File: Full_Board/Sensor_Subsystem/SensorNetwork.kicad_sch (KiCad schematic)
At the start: 34 parts, among them IC5 CD74HC4051PWT, IC6 CD74HC4051PWT, J12 OQ0432500000G, J13 OQ0432500000G, J14 OQ0432500000G, J15 OQ0432500000G, J16 OQ0432500000G, J17 OQ0432500000G, J18 OQ0432500000G, J19 OQ0432500000G, U13 UCLAMP3301H.TCT, U14 UCLAMP3301H.TCT

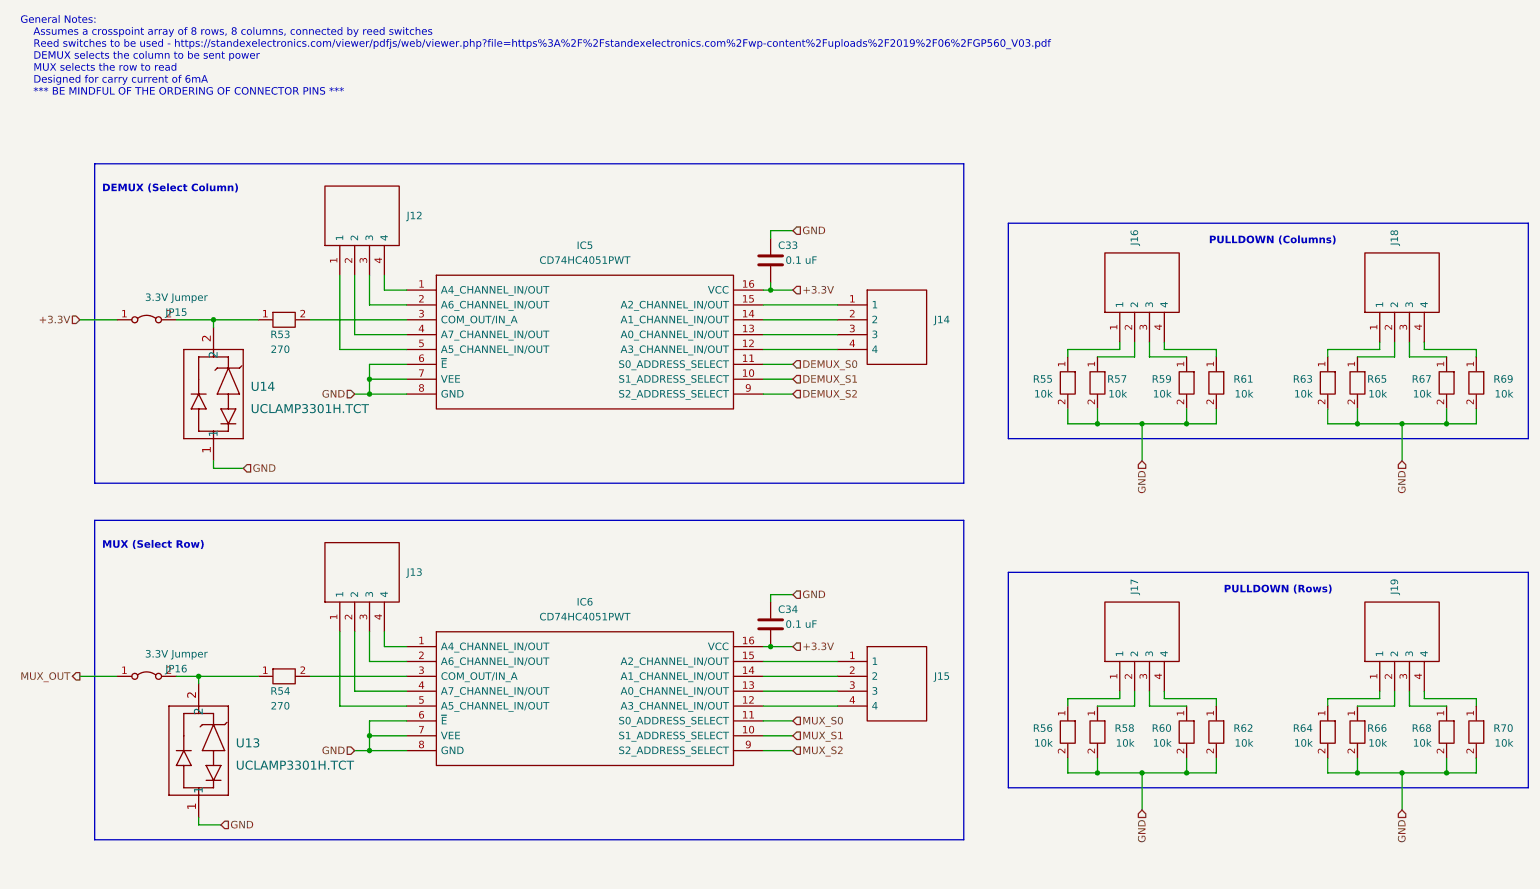
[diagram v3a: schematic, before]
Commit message: Replace small resistors/capacitors with through-hole; fix DRC aside from electromagnet and MUXes
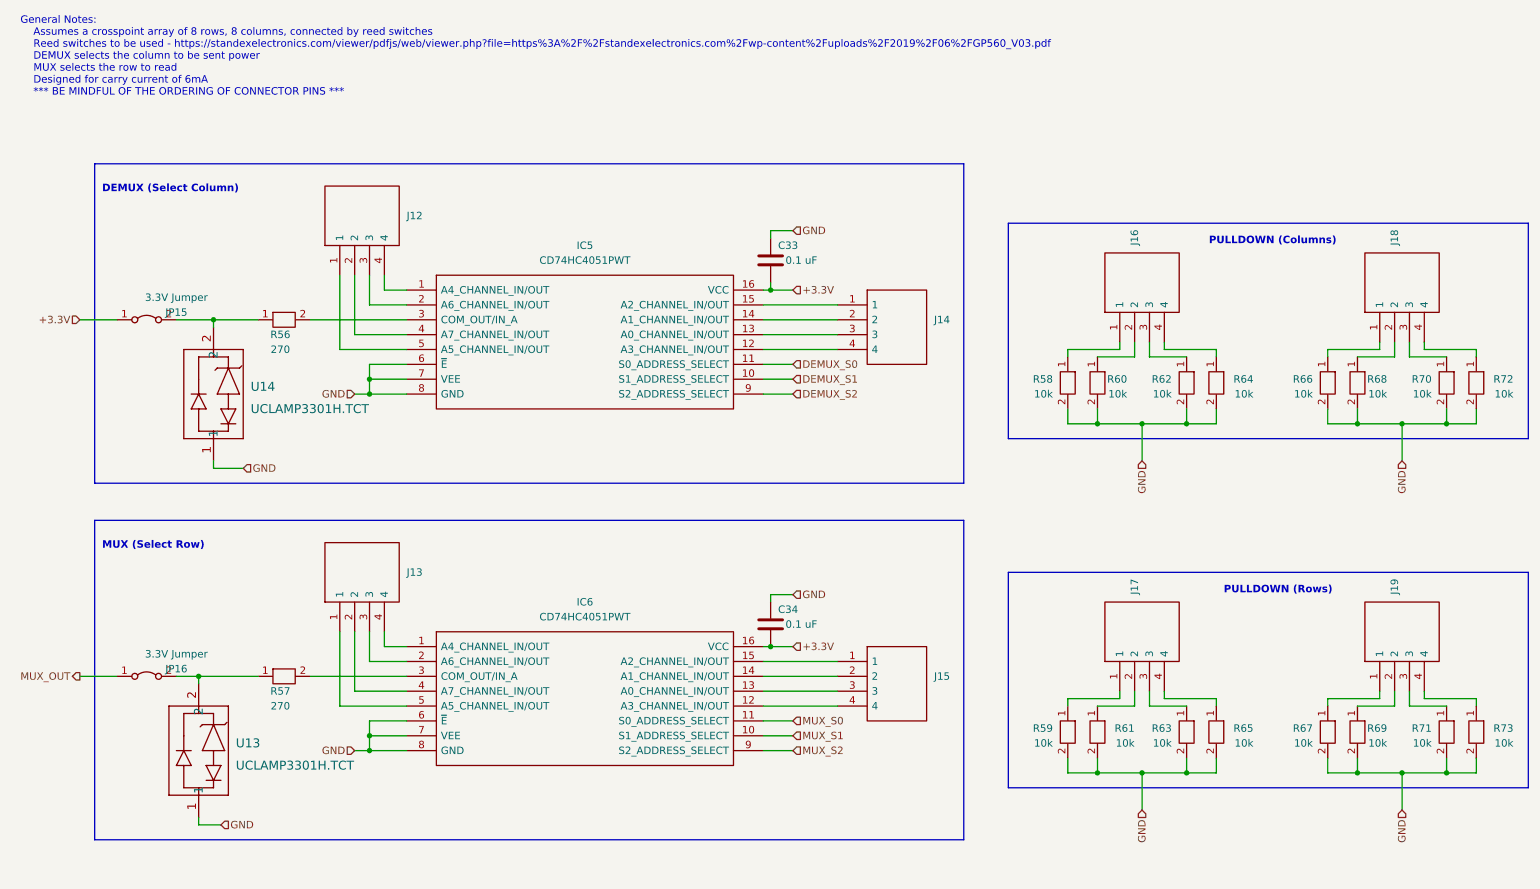
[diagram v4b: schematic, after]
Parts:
- IC5, IC6: Digikey Part Number (none) -> 296-32071-1-ND; Digikey link (none) -> https://www.digikey.com/en/products/detail/texas-instrument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; Height 1.2 -> (none); Manufacturer's Part Number (none) -> CD74HC4051PWT; Manufacturer_Name Texas Instruments -> (none); Manufacturer_Part_Number CD74HC4051PWT -> (none); Mouser Price/Stock https://www.mouser.co.uk/ProductDetail/Texas-Instruments/CD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 -> (none); Mouser link (none) -> https://www.mouser.com/ProductDetail/Texas-Instruments/CD74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
- renumbered R53 to R56, R54 to R57, R55 to R58, R56 to R59, R57 to R60, R58 to R61, R59 to R62, R60 to R63, R61 to R64, R62 to R65, R63 to R66, R64 to R67, R65 to R68, R66 to R69, R67 to R70, R68 to R71, R69 to R72, R70 to R73
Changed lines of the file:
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@@
   (symbol (lib_id "RMCF1206FT10K0:10k") (at 265.43 133.35 270) (unit 1)
     (in_bom yes) (on_board yes)
-    (property "Reference" "R70" (id 0) (at 271.78 137.16 90)
+    (property "Reference" "R73" (id 0) (at 271.78 137.16 90)
       (effects (font (size 1.27 1.27)) (justify right))
     )
@@
   (symbol (lib_id "RMCF1206FT10K0:10k") (at 260.35 133.35 270) (unit 1)
     (in_bom yes) (on_board yes)
-    (property "Reference" "R68" (id 0) (at 257.81 137.16 90)
+    (property "Reference" "R71" (id 0) (at 257.81 137.16 90)
       (effects (font (size 1.27 1.27)) (justify right))
     )
@@
   (symbol (lib_id "RMCF1206FT10K0:10k") (at 260.35 73.66 270) (unit 1)
     (in_bom yes) (on_board yes)
-    (property "Reference" "R67" (id 0) (at 257.81 77.47 90)
+    (property "Reference" "R70" (id 0) (at 257.81 77.47 90)
       (effects (font (size 1.27 1.27)) (justify right))
     )
@@
   (symbol (lib_id "RMCF1206FT10K0:10k") (at 195.58 73.66 270) (unit 1)
     (in_bom yes) (on_board yes)
-    (property "Reference" "R55" (id 0) (at 193.04 77.47 90)
+    (property "Reference" "R58" (id 0) (at 193.04 77.47 90)
       (effects (font (size 1.27 1.27)) (justify right))
     )
@@
   (symbol (lib_id "RMCF1206FT10K0:10k") (at 200.66 133.35 270) (unit 1)
     (in_bom yes) (on_board yes)
-    (property "Reference" "R58" (id 0) (at 207.01 137.16 90)
+    (property "Reference" "R61" (id 0) (at 207.01 137.16 90)
       (effects (font (size 1.27 1.27)) (justify right))
     )
@@
   (symbol (lib_id "SDR10EZPJ271:SDR10EZPJ271") (at 57.15 67.31 0) (unit 1)
     (in_bom yes) (on_board yes)
-    (property "Reference" "R53" (id 0) (at 60.96 69.85 0))
+    (property "Reference" "R56" (id 0) (at 60.96 69.85 0))
     (property "Value" "270" (id 1) (at 60.96 72.39 0))
     (property "Footprint" "SDR10EZPJ271:RESC2012X65N" (id 2) (at 71.12 66.04 0)
@@
   (symbol (lib_id "RMCF1206FT10K0:10k") (at 215.9 73.66 270) (unit 1)
     (in_bom yes) (on_board yes)
-    (property "Reference" "R59" (id 0) (at 213.36 77.47 90)
+    (property "Reference" "R62" (id 0) (at 213.36 77.47 90)
       (effects (font (size 1.27 1.27)) (justify right))
     )
@@
       (effects (font (size 1.27 1.27)) (justify left) hide)
     )
-    (property "Description" "High-speed CMOS 8-channel analog multiplexer & demultiplexer" (id 4) (at 139.7 125.73 0)
-      (effects (font (size 1.27 1.27)) (justify left) hide)
-    )
-    (property "Height" "1.2" (id 5) (at 139.7 128.27 0)
+    (property "Manufacturer's Part Number" "CD74HC4051PWT" (id 4) (at 139.7 138.43 0)
+      (effects (font (size 1.27 1.27)) (justify left) hide)
+    )
+    (property "Digikey Part Number" "296-32071-1-ND" (id 5) (at 139.7 125.73 0)
       (effects (font (size 1.27 1.27)) (justify left) hide)
     )
@@
       (effects (font (size 1.27 1.27)) (justify left) hide)
     )
-    (property "Mouser Price/Stock" "https://www.mouser.co.uk/ProductDetail/Texas-Instruments/CD74HC4051PWT?qs=xFfolx0DHx2HWIPlmtNafQ%3D%3D" (id 7) (at 139.7 133.35 0)
-      (effects (font (size 1.27 1.27)) (justify left) hide)
-    )
-    (property "Manufacturer_Name" "Texas Instruments" (id 8) (at 139.7 135.89 0)
-      (effects (font (size 1.27 1.27)) (justify left) hide)
-    )
-    (property "Manufacturer_Part_Number" "CD74HC4051PWT" (id 9) (at 139.7 138.43 0)
+    (property "Digikey link" "https://www.digikey.com/en/products/detail/texas-instruments/CD74HC4051PWT/1507172" (id 7) (at 139.7 128.27 0)
+      (effects (font (size 1.27 1.27)) (justify left) hide)
+    )
+    (property "Mouser link" "https://www.mouser.com/ProductDetail/Texas-Instruments/CD74HC4051PWT?qs=xFfolx0DHx2HWIPlmtNafQ%3D%3D" (id 8) (at 139.7 133.35 0)
       (effects (font (size 1.27 1.27)) (justify left) hide)
     )
@@
   (symbol (lib_id "RMCF1206FT10K0:10k") (at 265.43 73.66 270) (unit 1)
     (in_bom yes) (on_board yes)
-    (property "Reference" "R69" (id 0) (at 271.78 77.47 90)
+    (property "Reference" "R72" (id 0) (at 271.78 77.47 90)
       (effects (font (size 1.27 1.27)) (justify right))
     )
@@
   (symbol (lib_id "RMCF1206FT10K0:10k") (at 220.98 73.66 270) (unit 1)
     (in_bom yes) (on_board yes)
-    (property "Reference" "R61" (id 0) (at 227.33 77.47 90)
+    (property "Reference" "R64" (id 0) (at 227.33 77.47 90)
       (effects (font (size 1.27 1.27)) (justify right))
     )
@@
   (symbol (lib_id "RMCF1206FT10K0:10k") (at 245.11 73.66 270) (unit 1)
     (in_bom yes) (on_board yes)
-    (property "Reference" "R65" (id 0) (at 250.19 77.47 90)
+    (property "Reference" "R68" (id 0) (at 250.19 77.47 90)
       (effects (font (size 1.27 1.27)) (justify right))
     )
@@
   (symbol (lib_id "RMCF1206FT10K0:10k") (at 215.9 133.35 270) (unit 1)
     (in_bom yes) (on_board yes)
-    (property "Reference" "R60" (id 0) (at 213.36 137.16 90)
+    (property "Reference" "R63" (id 0) (at 213.36 137.16 90)
       (effects (font (size 1.27 1.27)) (justify right))
     )
@@
   (symbol (lib_id "RMCF1206FT10K0:10k") (at 200.66 73.66 270) (unit 1)
     (in_bom yes) (on_board yes)
-    (property "Reference" "R57" (id 0) (at 205.74 77.47 90)
+    (property "Reference" "R60" (id 0) (at 205.74 77.47 90)
       (effects (font (size 1.27 1.27)) (justify right))
     )
@@
     (pin "4")
   )
-  (symbol (lib_id "CD74HC4051PWT:CD74HC4051PWT") (at 82.55 62.23 0) (unit 1)
+  (symbol (lib_name "CD74HC4051PWT_1") (lib_id "CD74HC4051PWT:CD74HC4051PWT") (at 82.55 62.23 0) (unit 1)
     (in_bom yes) (on_board yes) (fields_autoplaced)
     (property "Reference" "IC5" (id 0) (at 113.03 54.61 0))
@@
       (effects (font (size 1.27 1.27)) (justify left) hide)
     )
-    (property "Description" "High-speed CMOS 8-channel analog multiplexer & demultiplexer" (id 4) (at 139.7 64.77 0)
-      (effects (font (size 1.27 1.27)) (justify left) hide)
-    )
-    (property "Height" "1.2" (id 5) (at 139.7 67.31 0)
+    (property "Manufacturer's Part Number" "CD74HC4051PWT" (id 9) (at 139.7 77.47 0)
+      (effects (font (size 1.27 1.27)) (justify left) hide)
+    )
+    (property "Digikey Part Number" "296-32071-1-ND" (id 4) (at 139.7 64.77 0)
       (effects (font (size 1.27 1.27)) (justify left) hide)
     )
@@
       (effects (font (size 1.27 1.27)) (justify left) hide)
     )
-    (property "Mouser Price/Stock" "https://www.mouser.co.uk/ProductDetail/Texas-Instruments/CD74HC4051PWT?qs=xFfolx0DHx2HWIPlmtNafQ%3D%3D" (id 7) (at 139.7 72.39 0)
-      (effects (font (size 1.27 1.27)) (justify left) hide)
-    )
-    (property "Manufacturer_Name" "Texas Instruments" (id 8) (at 139.7 74.93 0)
-      (effects (font (size 1.27 1.27)) (justify left) hide)
-    )
-    (property "Manufacturer_Part_Number" "CD74HC4051PWT" (id 9) (at 139.7 77.47 0)
+    (property "Digikey link" "https://www.digikey.com/en/products/detail/texas-instruments/CD74HC4051PWT/1507172" (id 5) (at 139.7 67.31 0)
+      (effects (font (size 1.27 1.27)) (justify left) hide)
+    )
+    (property "Mouser link" "https://www.mouser.com/ProductDetail/Texas-Instruments/CD74HC4051PWT?qs=xFfolx0DHx2HWIPlmtNafQ%3D%3D" (id 7) (at 139.7 72.39 0)
       (effects (font (size 1.27 1.27)) (justify left) hide)
     )
@@
   (symbol (lib_id "RMCF1206FT10K0:10k") (at 240.03 73.66 270) (unit 1)
     (in_bom yes) (on_board yes)
-    (property "Reference" "R63" (id 0) (at 237.49 77.47 90)
+    (property "Reference" "R66" (id 0) (at 237.49 77.47 90)
       (effects (font (size 1.27 1.27)) (justify right))
     )
@@
   (symbol (lib_id "RMCF1206FT10K0:10k") (at 245.11 133.35 270) (unit 1)
     (in_bom yes) (on_board yes)
-    (property "Reference" "R66" (id 0) (at 250.19 137.16 90)
+    (property "Reference" "R69" (id 0) (at 250.19 137.16 90)
       (effects (font (size 1.27 1.27)) (justify right))
     )
@@
   (symbol (lib_id "RMCF1206FT10K0:10k") (at 220.98 133.35 270) (unit 1)
     (in_bom yes) (on_board yes)
-    (property "Reference" "R62" (id 0) (at 227.33 137.16 90)
+    (property "Reference" "R65" (id 0) (at 227.33 137.16 90)
       (effects (font (size 1.27 1.27)) (justify right))
     )
@@
   (symbol (lib_id "SDR10EZPJ271:SDR10EZPJ271") (at 57.15 128.27 0) (unit 1)
     (in_bom yes) (on_board yes)
-    (property "Reference" "R54" (id 0) (at 60.96 130.81 0))
+    (property "Reference" "R57" (id 0) (at 60.96 130.81 0))
     (property "Value" "270" (id 1) (at 60.96 133.35 0))
     (property "Footprint" "SDR10EZPJ271:RESC2012X65N" (id 2) (at 71.12 127 0)
@@
   (symbol (lib_id "RMCF1206FT10K0:10k") (at 240.03 133.35 270) (unit 1)
     (in_bom yes) (on_board yes)
-    (property "Reference" "R64" (id 0) (at 237.49 137.16 90)
+    (property "Reference" "R67" (id 0) (at 237.49 137.16 90)
       (effects (font (size 1.27 1.27)) (justify right))
     )
@@
   (symbol (lib_id "RMCF1206FT10K0:10k") (at 195.58 133.35 270) (unit 1)
     (in_bom yes) (on_board yes)
-    (property "Reference" "R56" (id 0) (at 193.04 137.16 90)
-      (effects (font (size 1.27 1.27)) (justify right))
-    )
+    (property "Reference" "R59" (id 0) (at 193.04 137.16 90)
+      (effects (font (size 1.27 1.27)) (justify right))
+    )

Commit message: Replace MUX/DEMUX; DRC passes aside from electromagnet
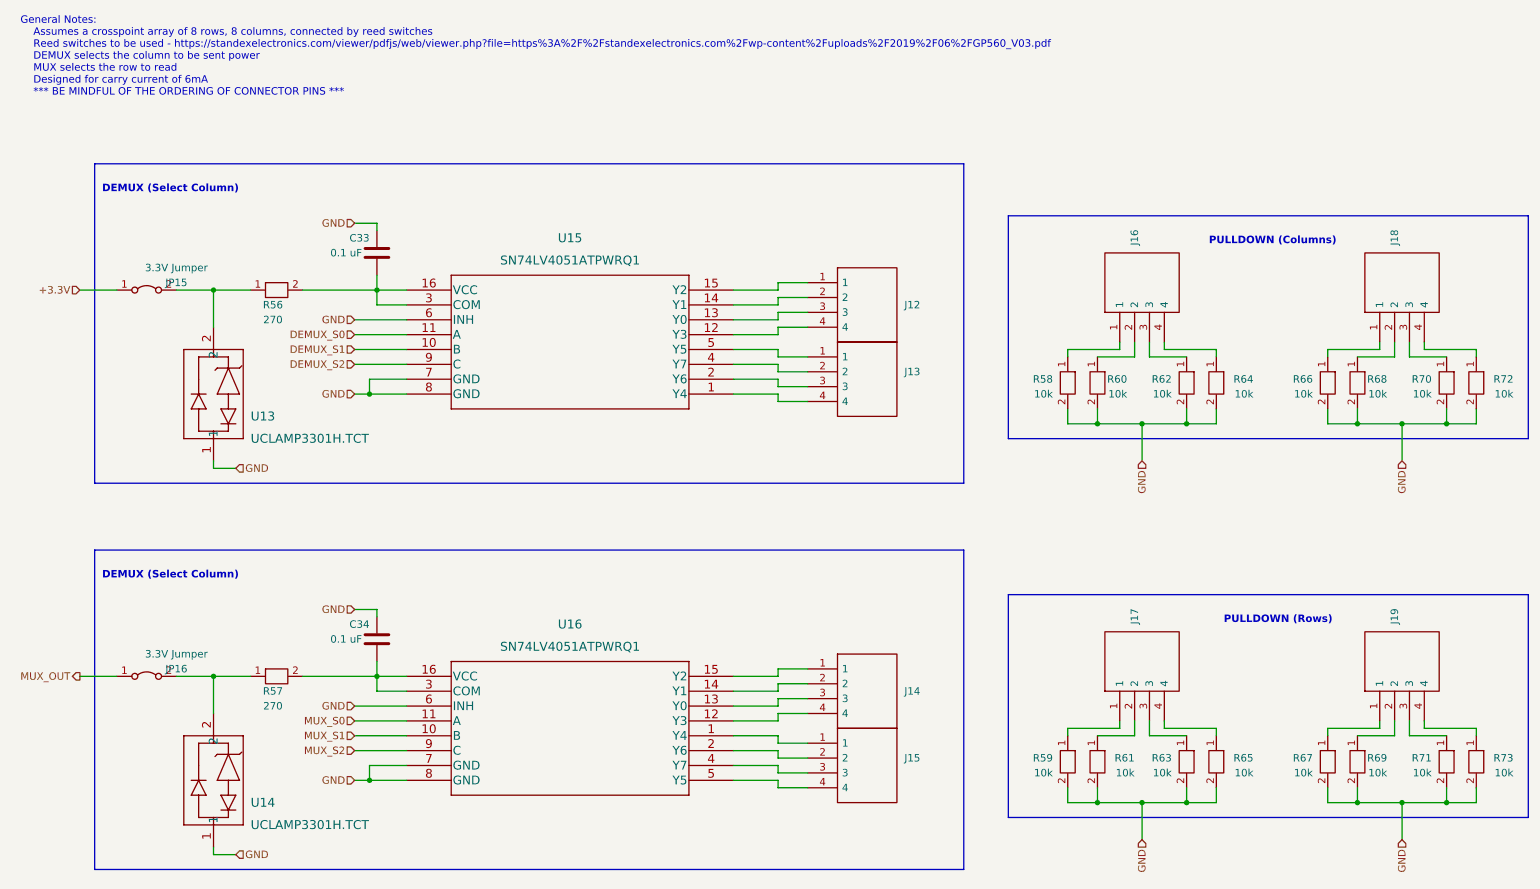
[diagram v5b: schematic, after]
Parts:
- removed IC5, IC6: CD74HC4051PWT, SOP65P640X120-16N, symbol CD74HC4051PWT:CD74HC4051PWT
- removed U13: UCLAMP3301H.TCT, UCLAMP3310H-TCT:UCLAMP3301H.TCT, symbol UCLAMP3301H-TCT:UCLAMP3301H.TCT
- added U14: UCLAMP3301H.TCT, UCLAMP3310H-TCT:UCLAMP3301H.TCT, symbol UCLAMP3301H-TCT:UCLAMP3301H.TCT
- added U15, U16: SN74LV4051ATPWRQ1, SN74LV4051ATPWRQ1:SN74LV4051ATPWRQ1, symbol SN74LV4051ATPWRQ1:SN74LV4051ATPWRQ1
- renumbered U14 to U13
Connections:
- net +3.3V: no longer C33.2, C34.2
- net DEMUX_S0: now also U15.11 (A)
- net DEMUX_S1: now also U15.10 (B)
- net DEMUX_S2: now also U15.9 (C)
- net GND: now also U14.1, U15.6 (INH), U15.7 (GND), U15.8 (GND), U16.6 (INH), U16.7 (GND), U16.8 (GND)
- net MUX_S0: now also U16.11 (A)
- net MUX_S1: now also U16.10 (B)
- net MUX_S2: now also U16.9 (C)
- net at J15.1: now also U16.1 (Y4)
- net at J15.2: now also U16.2 (Y6)
- net at J15.3: now also U16.4 (Y7)
- net at J15.4: now also U16.5 (Y5)
- net at JP16.2 (B), R57.1: now also U14.2
- net at J14.1: now also U16.15 (Y2)
- net at J14.2: now also U16.14 (Y1)
- net at J14.3: now also U16.13 (Y0)
- net at J14.4: now also U16.12 (Y3)
- net at R56.2: now also C33.2, U15.16 (VCC), U15.3 (COM)
- net at J13.4: now also U15.1 (Y4)
- net at J13.3: now also U15.2 (Y6)
- net at R57.2: now also C34.2, U16.16 (VCC), U16.3 (COM)
- net at J13.2: now also U15.4 (Y7)
- net at J13.1: now also U15.5 (Y5)
- net at J12.4: now also U15.12 (Y3)
- net at J12.3: now also U15.13 (Y0)
- net at J12.2: now also U15.14 (Y1)
- net at J12.1: now also U15.15 (Y2)
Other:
- note removed: "MUX (Select Row)"
- moved on the sheet: J17, J19, JP15, R56, R59, R61, R63, R65, R67, R69, R71, R73
